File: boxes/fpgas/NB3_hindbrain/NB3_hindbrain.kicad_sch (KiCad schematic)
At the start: 53 parts, among them IC1 FPGA_ICE40UP5K-SG48I, IC2 NOR_Flash_W25Q32JVSSIQ, J1 MicroUSB_10103594-0001LF, J2 Conn_01x20_Male, J3 Conn_01x20_Male, U1 EEPROM_93LC56BT-I-OT, U2 USBtoSPI_FT4232HL, Y1 Osc_12MHz_ECS-2520MV-120-BN-TR

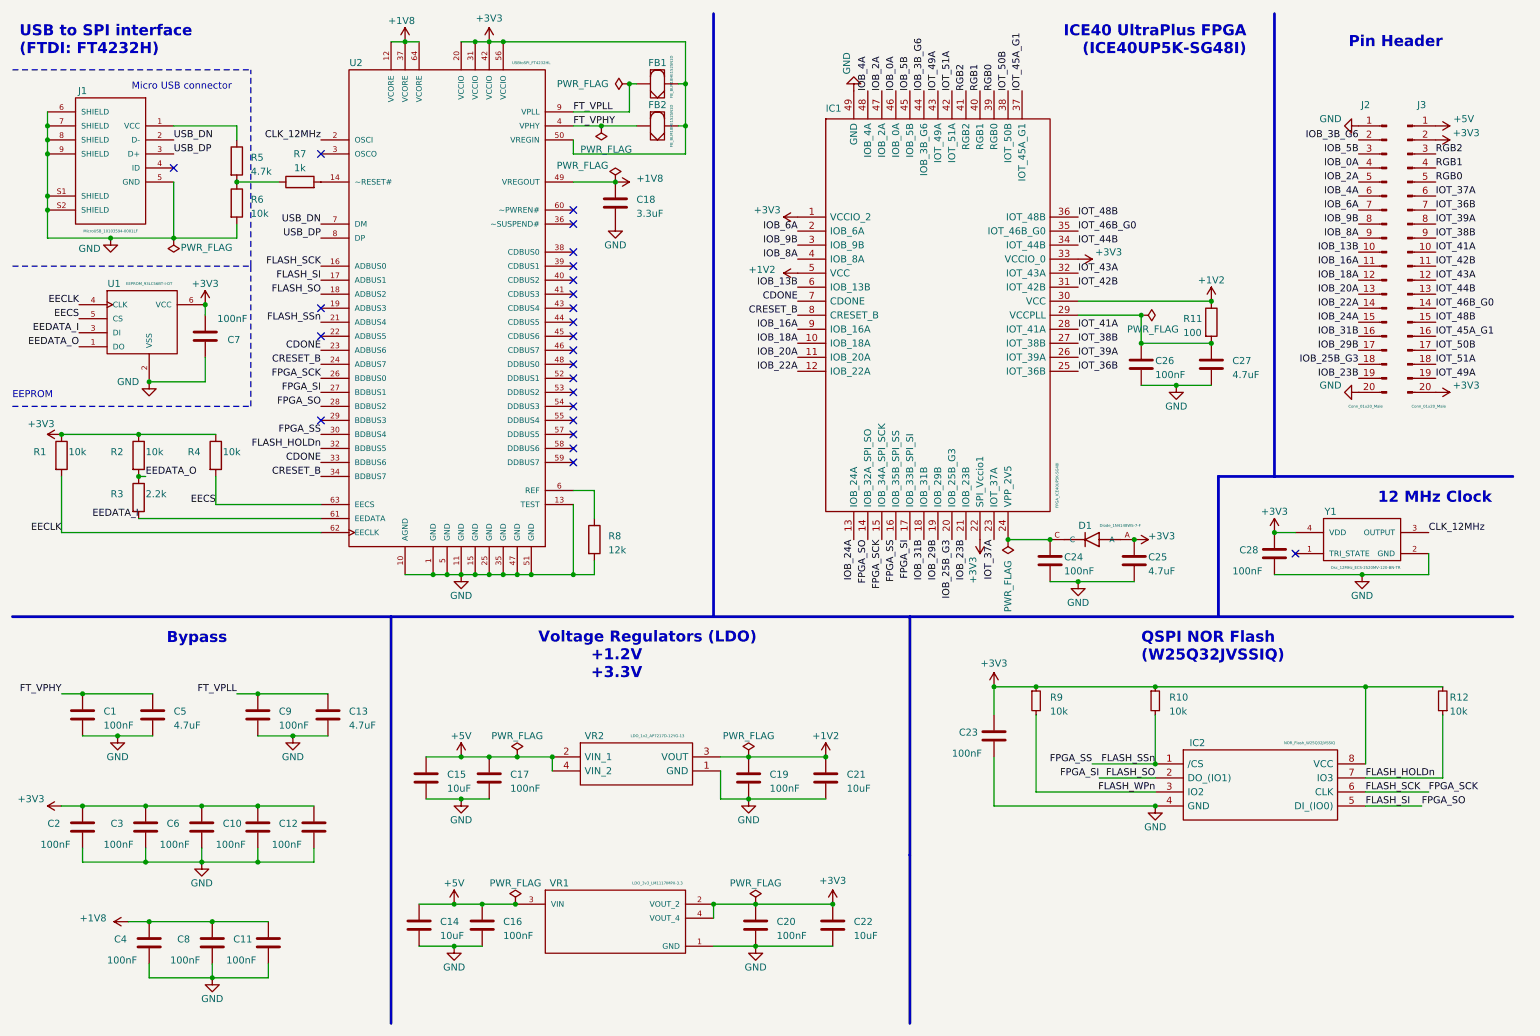
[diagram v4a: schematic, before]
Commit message: NB£_hindbrain PCB placement done
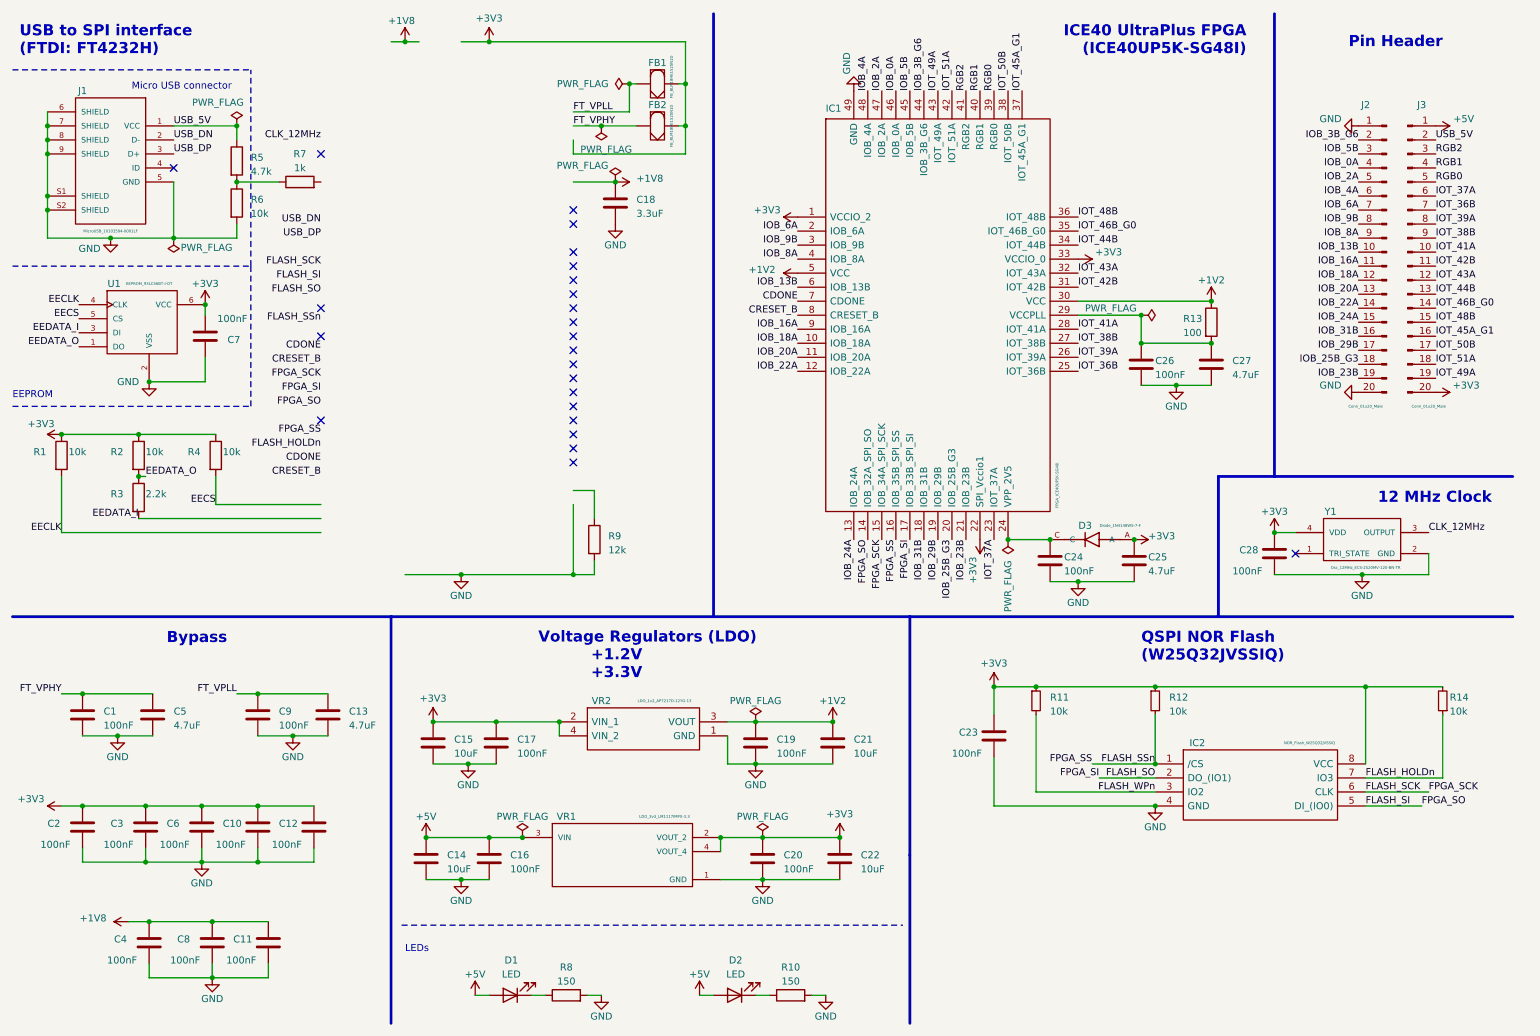
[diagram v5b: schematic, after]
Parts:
- removed U2: USBtoSPI_FT4232HL, NB3_hindbrain:USBtoSPI_FT4232HL, symbol NB3_hindbrain:USBtoSPI_FT4232HL
- added D1, D2: LED, LED_SMD:LED_0603_1608Metric, symbol Device:LED
- added R10, R8: 150, Resistor_SMD:R_0402_1005Metric, symbol Device:R
- renumbered D1 to D3, R9 to R11, R10 to R12, R11 to R13, R12 to R14, R8 to R9
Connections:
- net +3V3: now also C15.1, C17.1, VR2.2 (VIN_1), VR2.4 (VIN_2); no longer J3.2 (Pin_2)
- net +5V: now also D1.2 (A), D2.2 (A); no longer C15.1, C17.1, VR2.2 (VIN_1), VR2.4 (VIN_2)
- net GND: now also R10.2, R8.2
- net USB_5V: now reaches J1.1 (VCC), R5.1
- net USB_5V: now also J3.2 (Pin_2)
- new net: D2.1 (K), R10.1
- new net: D1.1 (K), R8.1
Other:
- note added: "LEDs"
- moved on the sheet: C14, C15, C16, C17, C19, C20, C21, C22, VR1, VR2
